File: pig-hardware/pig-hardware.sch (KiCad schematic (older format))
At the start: 29 parts, among them P1 PiB+_IO, P10 CONN_01X04, P2 CONN_01X04, P3 CONN_01X04, P4 CONN_01X02, P5 CONN_01X04, P6 CONN_01X08, P7 CONN_01X01, P8 CONN_01X02, P9 nrf24L01+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

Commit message: swapped pro with moteino
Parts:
- removed P10: CONN_01X04, Pin_Headers:Pin_Header_Straight_1x04, symbol CONN_01X04
- removed P7: CONN_01X01, Pin_Headers:Pin_Header_Straight_1x01, symbol CONN_01X01
- removed U1: ArduinoProMini-3v3, MyFootprints:Sparkfun-ArduinoProMini, symbol ArduinoProMini-3v3
- removed U3: RFM69HW, MyFootprints:RFM69, symbol RFM69HW
- added U1: Moteino, symbol Moteino
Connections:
- net +5V: now also U1.25 (VIN)
- net 3V3: no longer P5.3 (P3)
- net ATEMP: now also U1.21 (A7)
- net GND: now also U1.26 (GND)
- net LED: now also U1.7 (D7)
- net NRFCE: now also U1.4 (D4)
- net NRFCSN: now also U1.5 (D5)
- net NRFIRQ: now also U1.3 (D3)
- net ONEWIRE: now also U1.6 (D6)
- net PROMISO: now also U1.12 (D12_MI*)
- net PROMOSI: now also U1.11 (D11_MO*)
- net PRORX: now also U1.22 (RX)
- net PROSCK: now also U1.13 (D13_SCK*)
- net PROTX: now also U1.23 (TX)
- net SCL: now also U1.19 (A5_SCL)
- net SDA: now also U1.18 (A4_SDA)
- net SWRX1: now also U1.15 (A1)
- net SWRX2: now also U1.17 (A3)
- net SWTX1: now also U1.14 (A0)
- net SWTX2: now also U1.16 (A2)
- new net: P5.3 (P3), U1.24 (3v3)
- no-connect marks 22 -> 30
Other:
- note removed: "MOTEINO"
- moved on the sheet: P2, P3, P4, P5, P9

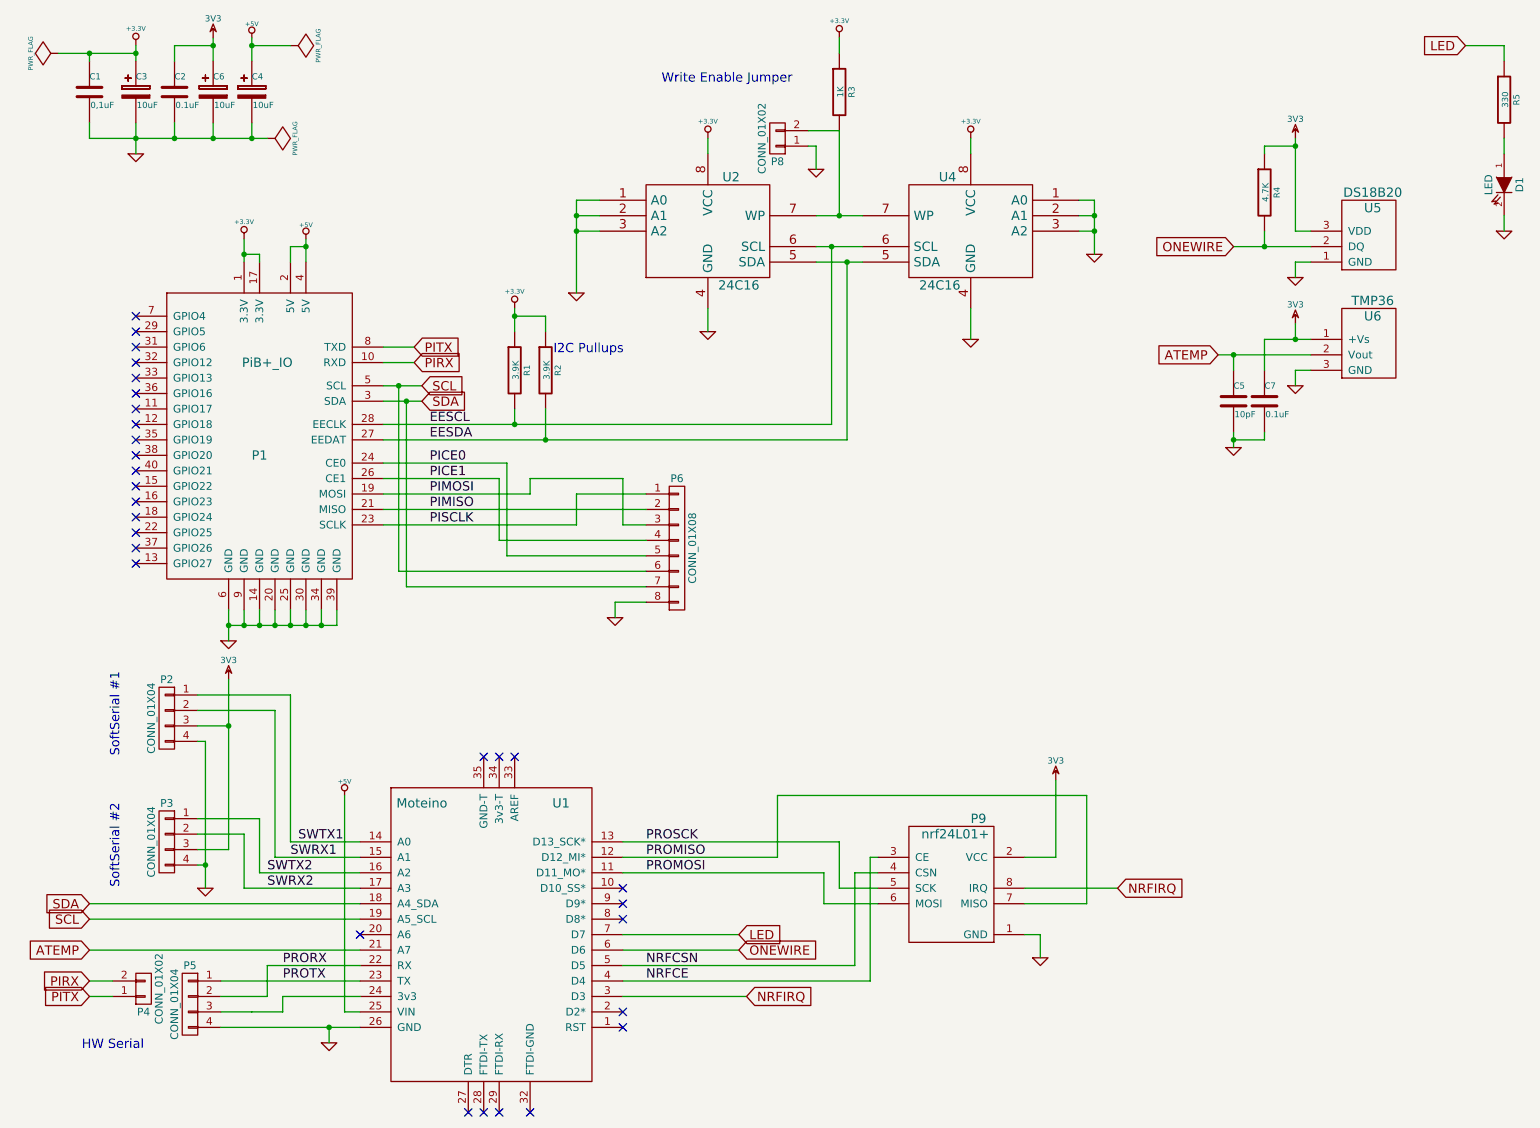
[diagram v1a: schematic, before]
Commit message: update pcb for moteino
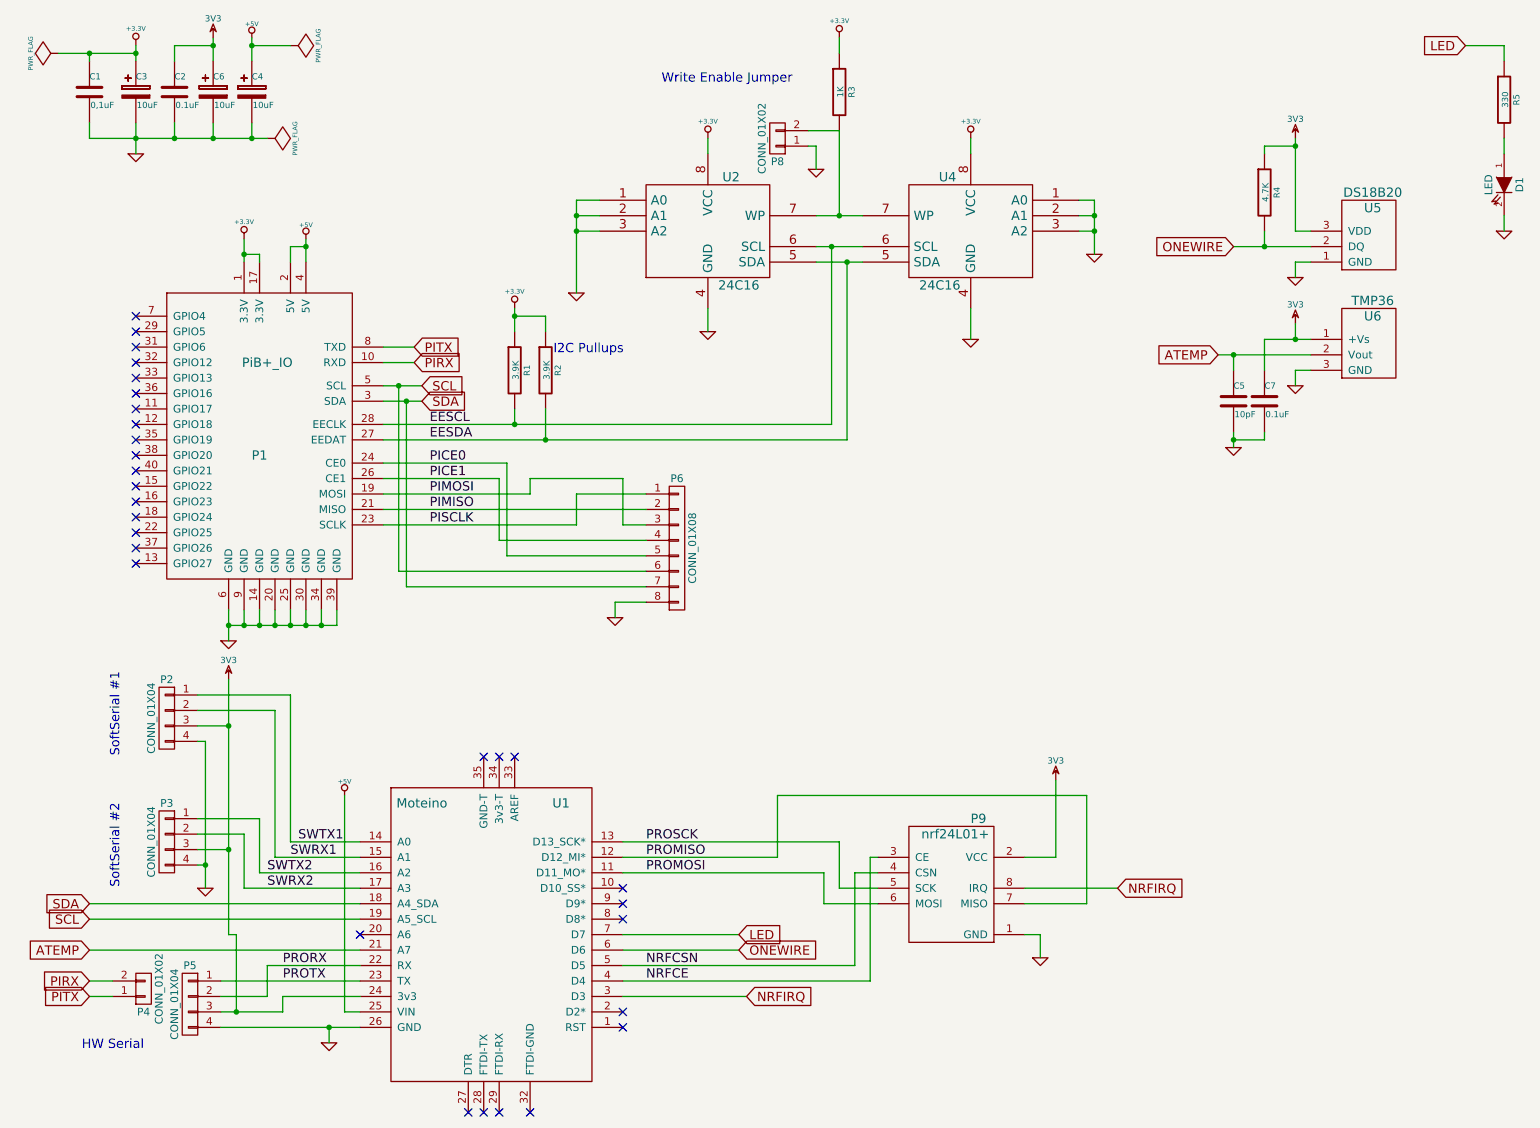
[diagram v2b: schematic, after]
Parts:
- U1: footprint (none) -> MyFootprints:Moteino
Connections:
- net 3V3: now also P5.3 (P3), U1.24 (3v3)
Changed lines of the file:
@@
 $EndComp
 Wire Wire Line
-	3000 3250 3850 3250
-Wire Wire Line
-	3850 3250 5900 3250
-Wire Wire Line
-	3000 3350 4050 3350
-Wire Wire Line
-	4050 3350 6000 3350
+	3000 3250 5900 3250
+Wire Wire Line
+	3000 3350 6000 3350
 Wire Wire Line
 	5100 2500 5100 2650
 Wire Wire Line
-	4250 1800 4250 1900
-Wire Wire Line
-	4250 1900 4250 2000
-Wire Wire Line
-	4250 2000 4250 2400
+	4250 1800 4250 2400
 Wire Wire Line
 	4400 1800 4250 1800
@@
 Connection ~ 4250 2000
 Wire Wire Line
-	1400 1300 1400 1400
-Wire Wire Line
-	1400 1400 1400 1500
+	1400 1300 1400 1500
 Wire Wire Line
 	2150 1400 2150 1300
 Wire Wire Line
-	1100 1400 1400 1400
-Wire Wire Line
-	1400 1400 1650 1400
-Wire Wire Line
-	1650 1400 1900 1400
-Wire Wire Line
-	1900 1400 2150 1400
-Wire Wire Line
-	2150 1400 2250 1400
+	1100 1400 2250 1400
 Connection ~ 1400 1400
 Wire Wire Line
-	2150 750  2150 800
-Wire Wire Line
-	2150 800  2150 900
-Wire Wire Line
-	1400 800  1400 850
-Wire Wire Line
-	1400 850  1400 900
-Wire Wire Line
-	900  850  1100 850
-Wire Wire Line
-	1100 850  1400 850
+	2150 750  2150 900
+Wire Wire Line
+	1400 800  1400 900
+Wire Wire Line
+	900  850  1400 850
 Connection ~ 1400 850
 Wire Wire Line
-	2100 2050 2100 2150
-Wire Wire Line
-	2100 2150 2100 2200
+	2100 2050 2100 2200
 Wire Wire Line
 	2200 2200 2200 2150
@@
 Connection ~ 2100 2150
 Wire Wire Line
-	2500 2050 2500 2100
-Wire Wire Line
-	2500 2100 2500 2200
+	2500 2050 2500 2200
 Wire Wire Line
 	2400 2200 2400 2100
@@
 	5950 1350 5950 1900
 Wire Wire Line
-	5800 1900 5950 1900
-Wire Wire Line
-	5950 1900 6100 1900
+	5800 1900 6100 1900
 Wire Wire Line
 	5950 850  5950 750
 Wire Wire Line
-	5800 2200 6000 2200
-Wire Wire Line
-	6000 2200 6100 2200
-Wire Wire Line
-	5800 2100 5900 2100
-Wire Wire Line
-	5900 2100 6100 2100
+	5800 2200 6100 2200
+Wire Wire Line
+	5800 2100 6100 2100
 Connection ~ 5950 1900
 Wire Wire Line
@@
 	7600 2000 7500 2000
 Wire Wire Line
-	7600 1800 7600 1900
-Wire Wire Line
-	7600 1900 7600 2000
-Wire Wire Line
-	7600 2000 7600 2150
+	7600 1800 7600 2150
 Wire Wire Line
 	7500 1800 7600 1800
@@
 $EndComp
 Wire Wire Line
-	2000 4450 2000 4550
-Wire Wire Line
-	2000 4550 2000 4650
+	2000 4450 2000 4650
 Wire Wire Line
 	2700 4550 2700 4450
 Wire Wire Line
-	2000 4550 2100 4550
-Wire Wire Line
-	2100 4550 2200 4550
-Wire Wire Line
-	2200 4550 2300 4550
-Wire Wire Line
-	2300 4550 2400 4550
-Wire Wire Line
-	2400 4550 2500 4550
-Wire Wire Line
-	2500 4550 2600 4550
-Wire Wire Line
-	2600 4550 2700 4550
+	2000 4550 2700 4550
 Connection ~ 2000 4550
 Wire Wire Line
@@
 $EndComp
 Wire Wire Line
-	3850 2500 3850 2550
-Wire Wire Line
-	3850 2550 3850 2650
+	3850 2500 3850 2650
 Wire Wire Line
 	4050 2650 4050 2550
@@
 SDA
 Wire Wire Line
-	3000 3000 3100 3000
-Wire Wire Line
-	3100 3000 3250 3000
-Wire Wire Line
-	3000 3100 3150 3100
-Wire Wire Line
-	3150 3100 3250 3100
-Wire Wire Line
-	8700 2700 8900 2700
-Wire Wire Line
-	8900 2700 9000 2700
+	3000 3000 3250 3000
+Wire Wire Line
+	3000 3100 3250 3100
+Wire Wire Line
+	8700 2700 9000 2700
 Wire Wire Line
 	8900 2700 8900 2600
@@
 	8900 2000 9000 2000
 Wire Wire Line
-	8900 1400 8900 1450
-Wire Wire Line
-	8900 1450 8900 2000
+	8900 1400 8900 2000
 Wire Wire Line
 	9000 2200 8900 2200
@@
 $EndComp
 Wire Wire Line
-	8500 3300 8500 3350
-Wire Wire Line
-	8500 3350 8500 3400
+	8500 3300 8500 3400
 Wire Wire Line
 	4550 5950 5950 5950
@@
 Connection ~ 8900 1450
 Wire Wire Line
-	8500 2100 8700 2100
-Wire Wire Line
-	8700 2100 9000 2100
+	8500 2100 9000 2100
 Wire Wire Line
 	8700 2000 8700 2100
 Connection ~ 8700 2100
 Wire Wire Line
-	8400 2800 8500 2800
-Wire Wire Line
-	8500 2800 9000 2800
+	8400 2800 9000 2800
 Wire Wire Line
 	8500 2900 8500 2800
@@
 	7350 5550 7350 6050
 $Comp
-L GND #PWR027
+L GND #PWR026
 U 1 1 549916D5
 P 7250 6700
-F 0 "#PWR027" H 7250 6700 30  0001 C CNN
+F 0 "#PWR026" H 7250 6700 30  0001 C CNN
 F 1 "GND" H 7250 6630 30  0001 C CNN
 F 2 "" H 7250 6700 60  0000 C CNN
@@
 	1100 1300 1100 1400
 $Comp
-L +5V #PWR028
+L +5V #PWR027
 U 1 1 54995222
 P 2750 5650
-F 0 "#PWR028" H 2750 5740 20  0001 C CNN
+F 0 "#PWR027" H 2750 5740 20  0001 C CNN
 F 1 "+5V" H 2750 5740 30  0000 C CNN
 F 2 "" H 2750 5650 60  0000 C CNN
@@
 	2750 7050 2750 5650
 $Comp
-L GND #PWR031
+L GND #PWR028
 U 1 1 54995516
 P 2650 7250
-F 0 "#PWR031" H 2650 7250 30  0001 C CNN
+F 0 "#PWR028" H 2650 7250 30  0001 C CNN
 F 1 "GND" H 2650 7180 30  0001 C CNN
 F 2 "" H 2650 7250 60  0000 C CNN
@@
 	1950 6950 2250 6950
 Wire Wire Line
-	1950 7050 2150 7050
-Wire Wire Line
-	2150 7050 2350 7050
+	1950 7050 2350 7050
 Wire Wire Line
 	6200 6150 6050 6150
@@
 PRORX
 $Comp
-L 3V3 #PWR033
+L 3V3 #PWR029
 U 1 1 54998898
 P 2000 4900
-F 0 "#PWR033" H 2000 5000 40  0001 C CNN
+F 0 "#PWR029" H 2000 5000 40  0001 C CNN
 F 1 "3V3" H 2000 5025 40  0000 C CNN
 F 2 "" H 2000 4900 60  0000 C CNN
@@
 	1800 5200 2000 5200
 Wire Wire Line
-	2000 4900 2000 5200
-Wire Wire Line
-	2000 5200 2000 6000
+	2000 4900 2000 6550
 Wire Wire Line
 	2000 6000 1800 6000
 Connection ~ 2000 5200
 $Comp
-L GND #PWR034
+L GND #PWR030
 U 1 1 54998BBD
 P 1850 6250
-F 0 "#PWR034" H 1850 6250 30  0001 C CNN
+F 0 "#PWR030" H 1850 6250 30  0001 C CNN
 F 1 "GND" H 1850 6180 30  0001 C CNN
 F 2 "" H 1850 6250 60  0000 C CNN
@@
 	1800 5300 1850 5300
 Wire Wire Line
-	1850 5300 1850 6100
-Wire Wire Line
-	1850 6100 1850 6250
+	1850 5300 1850 6250
 Wire Wire Line
 	1800 6100 1850 6100
@@
 $EndComp
 $Comp
-L GND #PWR035
+L GND #PWR031
 U 1 1 5499A65B
 P 4500 4500
-F 0 "#PWR035" H 4500 4500 30  0001 C CNN
+F 0 "#PWR031" H 4500 4500 30  0001 C CNN
 F 1 "GND" H 4500 4430 30  0001 C CNN
 F 2 "" H 4500 4500 60  0000 C CNN
@@
 Connection ~ 1900 1400
 $Comp
-L 3V3 #PWR036
+L 3V3 #PWR032
 U 1 1 5499F885
 P 1900 750
-F 0 "#PWR036" H 1900 850 40  0001 C CNN
+F 0 "#PWR032" H 1900 850 40  0001 C CNN
 F 1 "3V3" H 1900 875 40  0000 C CNN
 F 2 "" H 1900 750 60  0000 C CNN
@@
 $EndComp
 Wire Wire Line
-	1900 750  1900 800
-Wire Wire Line
-	1900 800  1900 900
+	1900 750  1900 900
 NoConn ~ 1400 4150
 NoConn ~ 1400 4050
@@
 F 0 "U1" H 4150 7400 60  0000 C CNN
 F 1 "Moteino" H 3250 7400 60  0000 C CNN
-F 2 "" H 3750 6550 60  0000 C CNN
+F 2 "MyFootprints:Moteino" H 3750 6550 60  0001 C CNN
 F 3 "" H 3750 6550 60  0000 C CNN
 	1    3750 6550
@@
 $EndComp
 Wire Wire Line
-	1950 7150 2650 7150
-Wire Wire Line
-	2650 7150 2850 7150
+	1950 7150 2850 7150
 Wire Wire Line
 	2650 7150 2650 7250
@@
 NoConn ~ 3650 7700
 NoConn ~ 3550 7700
+Wire Wire Line
+	2050 7050 2050 6550
+Wire Wire Line
+	2050 6550 2000 6550
+Connection ~ 2000 6000
+Connection ~ 2050 7050
 $EndSCHEMATC
